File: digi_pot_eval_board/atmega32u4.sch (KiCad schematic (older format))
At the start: 39 parts, among them J3 47346-0001, J4 DS-210, J5 DIN-5-OOTDTY, J6 DIN-5-OOTDTY, J7 JST-04, J8 DS1013-06S, Q1 BSS84, Q2 BSS84, U10 6N138, U11 NCP1117ST50T3G, U12 ATmega32U4-AU, U9 USBLC6-2SC6, Y1 16MHz HC-49SM

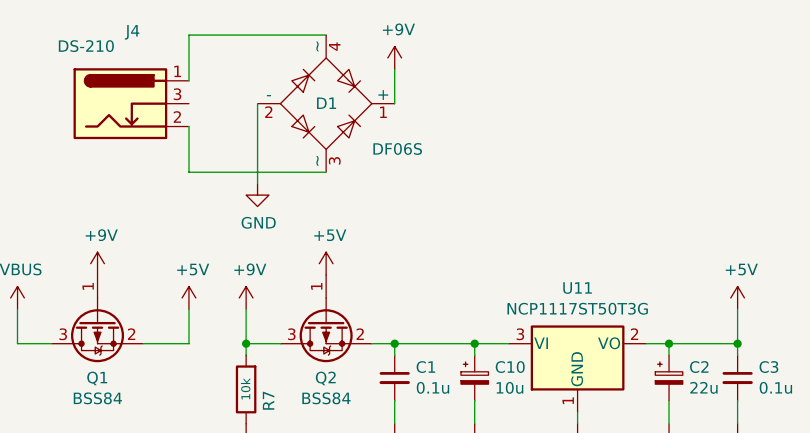
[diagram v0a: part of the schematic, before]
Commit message: Fixing MIDI optocoupler protection diode footprint.
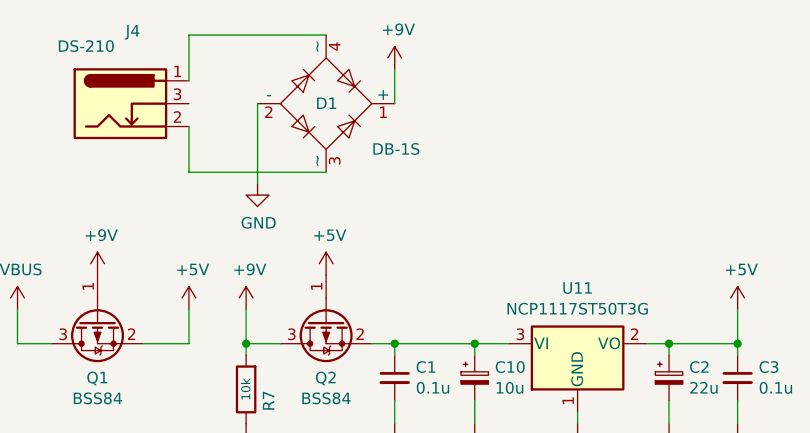
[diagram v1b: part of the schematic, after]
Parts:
- D1: value DF06S -> DB-1S
- D2: footprint Diode_SMD:D_SMA_Handsoldering -> Diode_SMD:D_SMA
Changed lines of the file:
@@
 EESchema Schematic File Version 4
-LIBS:digi_pot_eval_board-cache
 EELAYER 26 0
 EELAYER END
@@
 P 2200 1200
 F 0 "D1" H 2250 1200 50  0000 R CNN
-F 1 "DF06S" H 2400 1400 50  0000 L CNN
+F 1 "DB-1S" H 2400 1400 50  0000 L CNN
 F 2 "Diode_SMD:Diode_Bridge_Vishay_DFS" H 2200 1200 50  0001 C CNN
 F 3 "~" H 2200 1200 50  0001 C CNN
@@
 F 0 "D2" V 2304 5529 50  0000 L CNN
 F 1 "HS1D" V 2395 5529 50  0000 L CNN
-F 2 "Diode_SMD:D_SMA_Handsoldering" H 2350 5450 50  0001 C CNN
+F 2 "Diode_SMD:D_SMA" H 2350 5450 50  0001 C CNN
 F 3 "~" H 2350 5450 50  0001 C CNN
 	1    2350 5450

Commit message: Before wide nav_panel and Level pot move.
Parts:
- added J11: Conn_01x02_Male, Connector_JST:JST_EH_B02B-EH-A_1x02_P2.50mm_Vertical, symbol Connector:Conn_01x02_Male
- added J12: Conn_01x03_Male, Connector_JST:JST_EH_B03B-EH-A_1x03_P2.50mm_Vertical, symbol Connector:Conn_01x03_Male
- added J13: Conn_01x06_Male, Connector_JST:JST_EH_B06B-EH-A_1x06_P2.50mm_Vertical, symbol Connector:Conn_01x06_Male
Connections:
- net labels added: MIN4, MIN5, MOUT4, MOUT5
- wire segments 109 -> 118
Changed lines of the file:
@@
 EESchema Schematic File Version 4
+LIBS:digi_pot_eval_board-cache
 EELAYER 26 0
 EELAYER END
@@
 Wire Wire Line
 	2850 2500 2850 2600
+Text GLabel 1300 5300 0    50   Input ~ 0
+MIN5
+Text GLabel 2000 5300 3    50   Input ~ 0
+MIN4
+Wire Wire Line
+	1300 5300 1400 5300
+Connection ~ 1400 5300
+Text GLabel 4800 5500 3    50   Input ~ 0
+MOUT5
+Text GLabel 5400 5500 3    50   Input ~ 0
+MOUT4
+Wire Wire Line
+	4800 5500 4800 5400
+Connection ~ 4800 5400
+Wire Wire Line
+	5400 5500 5400 5400
+Connection ~ 5400 5400
+$Comp
+L Connector:Conn_01x02_Male J11
+U 1 1 5DB1A299
+P 1600 6100
+F 0 "J11" H 1706 6278 50  0000 C CNN
+F 1 "Conn_01x02_Male" H 1706 6187 50  0000 C CNN
+F 2 "Connector_JST:JST_EH_B02B-EH-A_1x02_P2.50mm_Vertical" H 1600 6100 50  0001 C CNN
+F 3 "~" H 1600 6100 50  0001 C CNN
+	1    1600 6100
+	1    0    0    -1
+$EndComp
+$Comp
+L Connector:Conn_01x03_Male J12
+U 1 1 5DB1A3AD
+P 4900 6300
+F 0 "J12" H 5006 6578 50  0000 C CNN
+F 1 "Conn_01x03_Male" H 5006 6487 50  0000 C CNN
+F 2 "Connector_JST:JST_EH_B03B-EH-A_1x03_P2.50mm_Vertical" H 4900 6300 50  0001 C CNN
+F 3 "~" H 4900 6300 50  0001 C CNN
+	1    4900 6300
+	1    0    0    -1
+$EndComp
+Text GLabel 6300 4050 2    50   Input ~ 0
+MOSI
+Text GLabel 6300 4150 2    50   Input ~ 0
+MISO
+Text GLabel 6300 4250 2    50   Input ~ 0
+SCK
+$Comp
+L Connector:Conn_01x06_Male J13
+U 1 1 5DB1DFAE
+P 6100 4250
+F 0 "J13" H 6206 4628 50  0000 C CNN
+F 1 "Conn_01x06_Male" H 6206 4537 50  0000 C CNN
+F 2 "Connector_JST:JST_EH_B06B-EH-A_1x06_P2.50mm_Vertical" H 6100 4250 50  0001 C CNN
+F 3 "~" H 6100 4250 50  0001 C CNN
+	1    6100 4250
+	1    0    0    -1
+$EndComp
+$Comp
+L power:+5V #PWR0180
+U 1 1 5DB1E025
+P 6800 4350
+F 0 "#PWR0180" H 6800 4200 50  0001 C CNN
+F 1 "+5V" H 6815 4523 50  0000 C CNN
+F 2 "" H 6800 4350 50  0001 C CNN
+F 3 "" H 6800 4350 50  0001 C CNN
+	1    6800 4350
+	1    0    0    -1
+$EndComp
+$Comp
+L power:GND #PWR0181
+U 1 1 5DB1E084
+P 6800 4600
+F 0 "#PWR0181" H 6800 4350 50  0001 C CNN
+F 1 "GND" H 6805 4427 50  0000 C CNN
+F 2 "" H 6800 4600 50  0001 C CNN
+F 3 "" H 6800 4600 50  0001 C CNN
+	1    6800 4600
+	1    0    0    -1
+$EndComp
+Wire Wire Line
+	6300 4550 6800 4550
+Wire Wire Line
+	6800 4550 6800 4600
+Wire Wire Line
+	6800 4350 6800 4450
+Wire Wire Line
+	6800 4450 6300 4450
+$Comp
+L power:GND #PWR0182
+U 1 1 5DB24EBB
+P 5550 6450
+F 0 "#PWR0182" H 5550 6200 50  0001 C CNN
+F 1 "GND" H 5555 6277 50  0000 C CNN
+F 2 "" H 5550 6450 50  0001 C CNN
+F 3 "" H 5550 6450 50  0001 C CNN
+	1    5550 6450
+	1    0    0    -1
+$EndComp
+Text GLabel 5100 6200 2    50   Input ~ 0
+MOUT5
+Text GLabel 5100 6400 2    50   Input ~ 0
+MOUT4
+Wire Wire Line
+	5100 6300 5550 6300
+Wire Wire Line
+	5550 6300 5550 6450
+Text GLabel 1800 6100 2    50   Input ~ 0
+MIN5
+Text GLabel 1800 6200 2    50   Input ~ 0
+MIN4
 $EndSCHEMATC

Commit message: Introducing new layout.
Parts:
- removed J11: Conn_01x02_Male, Connector_JST:JST_EH_B02B-EH-A_1x02_P2.50mm_Vertical, symbol Connector:Conn_01x02_Male
- removed J12: Conn_01x03_Male, Connector_JST:JST_EH_B03B-EH-A_1x03_P2.50mm_Vertical, symbol Connector:Conn_01x03_Male
- added J10: Conn_01x02_Male, Connector_JST:JST_EH_B02B-EH-A_1x02_P2.50mm_Vertical, symbol Connector:Conn_01x02_Male
- added J9: Conn_01x05_Male, Connector_JST:JST_EH_B05B-EH-A_1x05_P2.50mm_Vertical, symbol Connector:Conn_01x05_Male
- J4: footprint Connector_BarrelJack:BarrelJack_Wuerth_6941xx301002 -> (none)
- J5, J6: footprint Connectors:DIN5MIDI-OOTDTY -> (none)
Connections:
- net labels added: POW1, POW2
- wire segments 118 -> 120
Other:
- moved on the sheet: J4
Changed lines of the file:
@@
 L Connector:Barrel_Jack_Switch J4
 U 1 1 5D90FDCF
-P 1300 1200
-F 0 "J4" H 1355 1517 50  0000 C CNN
-F 1 "DS-210" H 1150 1450 50  0000 C CNN
-F 2 "Connector_BarrelJack:BarrelJack_Wuerth_6941xx301002" H 1350 1160 50  0001 C CNN
-F 3 "~" H 1350 1160 50  0001 C CNN
-	1    1300 1200
+P 900 1200
+F 0 "J4" H 955 1517 50  0000 C CNN
+F 1 "DS-210" H 750 1450 50  0000 C CNN
+F 2 "" H 950 1160 50  0001 C CNN
+F 3 "~" H 950 1160 50  0001 C CNN
+	1    900  1200
 	1    0    0    -1
 $EndComp
@@
 F 0 "J6" H 5100 4933 50  0000 C CNN
 F 1 "DIN-5-OOTDTY" H 5100 5024 50  0000 C CNN
-F 2 "Connectors:DIN5MIDI-OOTDTY" H 5100 5300 50  0001 C CNN
+F 2 "" H 5100 5300 50  0001 C CNN
 F 3 "http://www.mouser.com/ds/2/18/40_c091_abd_e-75918.pdf" H 5100 5300 50  0001 C CNN
 	1    5100 5300
@@
 F 0 "J5" H 1700 4833 50  0000 C CNN
 F 1 "DIN-5-OOTDTY" H 1700 4924 50  0000 C CNN
-F 2 "Connectors:DIN5MIDI-OOTDTY" H 1700 5200 50  0001 C CNN
+F 2 "" H 1700 5200 50  0001 C CNN
 F 3 "http://www.mouser.com/ds/2/18/40_c091_abd_e-75918.pdf" H 1700 5200 50  0001 C CNN
 	1    1700 5200
@@
 	5400 5500 5400 5400
 Connection ~ 5400 5400
-$Comp
-L Connector:Conn_01x02_Male J11
-U 1 1 5DB1A299
-P 1600 6100
-F 0 "J11" H 1706 6278 50  0000 C CNN
-F 1 "Conn_01x02_Male" H 1706 6187 50  0000 C CNN
-F 2 "Connector_JST:JST_EH_B02B-EH-A_1x02_P2.50mm_Vertical" H 1600 6100 50  0001 C CNN
-F 3 "~" H 1600 6100 50  0001 C CNN
-	1    1600 6100
-	1    0    0    -1
-$EndComp
-$Comp
-L Connector:Conn_01x03_Male J12
-U 1 1 5DB1A3AD
-P 4900 6300
-F 0 "J12" H 5006 6578 50  0000 C CNN
-F 1 "Conn_01x03_Male" H 5006 6487 50  0000 C CNN
-F 2 "Connector_JST:JST_EH_B03B-EH-A_1x03_P2.50mm_Vertical" H 4900 6300 50  0001 C CNN
-F 3 "~" H 4900 6300 50  0001 C CNN
-	1    4900 6300
-	1    0    0    -1
-$EndComp
 Text GLabel 6300 4050 2    50   Input ~ 0
 MOSI
@@
 Wire Wire Line
 	6800 4450 6300 4450
+Text GLabel 1550 1100 0    50   Input ~ 0
+POW1
+Wire Wire Line
+	1550 1100 1600 1100
+Text GLabel 1550 1300 0    50   Input ~ 0
+POW2
+Wire Wire Line
+	1550 1300 1600 1300
+$Comp
+L Connector:Conn_01x02_Male J10
+U 1 1 5DB811AD
+P 3650 1100
+F 0 "J10" H 3756 1278 50  0000 C CNN
+F 1 "Conn_01x02_Male" H 3756 1187 50  0000 C CNN
+F 2 "Connector_JST:JST_EH_B02B-EH-A_1x02_P2.50mm_Vertical" H 3650 1100 50  0001 C CNN
+F 3 "~" H 3650 1100 50  0001 C CNN
+	1    3650 1100
+	-1   0    0    -1
+$EndComp
+Text GLabel 3450 1100 0    50   Input ~ 0
+POW1
+Text GLabel 3450 1200 0    50   Input ~ 0
+POW2
+$Comp
+L Connector:Conn_01x05_Male J9
+U 1 1 5DB82855
+P 2700 6750
+F 0 "J9" H 2806 7128 50  0000 C CNN
+F 1 "Conn_01x05_Male" H 2806 7037 50  0000 C CNN
+F 2 "Connector_JST:JST_EH_B05B-EH-A_1x05_P2.50mm_Vertical" H 2700 6750 50  0001 C CNN
+F 3 "~" H 2700 6750 50  0001 C CNN
+	1    2700 6750
+	1    0    0    -1
+$EndComp
+Text GLabel 2900 6850 2    50   Input ~ 0
+MIN5
+Text GLabel 2900 6950 2    50   Input ~ 0
+MIN4
+Text GLabel 2900 6550 2    50   Input ~ 0
+MOUT5
+Text GLabel 2900 6750 2    50   Input ~ 0
+MOUT4
 $Comp
 L power:GND #PWR0182
-U 1 1 5DB24EBB
-P 5550 6450
-F 0 "#PWR0182" H 5550 6200 50  0001 C CNN
-F 1 "GND" H 5555 6277 50  0000 C CNN
-F 2 "" H 5550 6450 50  0001 C CNN
-F 3 "" H 5550 6450 50  0001 C CNN
-	1    5550 6450
-	1    0    0    -1
-$EndComp
-Text GLabel 5100 6200 2    50   Input ~ 0
-MOUT5
-Text GLabel 5100 6400 2    50   Input ~ 0
-MOUT4
-Wire Wire Line
-	5100 6300 5550 6300
-Wire Wire Line
-	5550 6300 5550 6450
-Text GLabel 1800 6100 2    50   Input ~ 0
-MIN5
-Text GLabel 1800 6200 2    50   Input ~ 0
-MIN4
+U 1 1 5DB82A46
+P 3400 6700
+F 0 "#PWR0182" H 3400 6450 50  0001 C CNN
+F 1 "GND" H 3405 6527 50  0000 C CNN
+F 2 "" H 3400 6700 50  0001 C CNN
+F 3 "" H 3400 6700 50  0001 C CNN
+	1    3400 6700
+	1    0    0    -1
+$EndComp
+Wire Wire Line
+	2900 6650 3400 6650
+Wire Wire Line
+	3400 6650 3400 6700
 $EndSCHEMATC

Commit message: Printed and tested layout version.
USB still on upper board.
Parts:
- removed D3: LED, LED_THT:LED_D5.0mm, symbol Device:LED
- removed J3: 47346-0001, Connector_USB:USB_Micro-B_Molex_47346-0001, symbol Connector:USB_B_Micro
- removed J4: DS-210, symbol Connector:Barrel_Jack_Switch
- removed J7: JST-04, Connector_JST:JST_EH_B04B-EH-A_1x04_P2.50mm_Vertical, symbol Connector:Conn_01x04_Male
- added J11, J12, J7: Conn_01x02_Male, Connector_JST:JST_EH_B02B-EH-A_1x02_P2.50mm_Vertical, symbol Connector:Conn_01x02_Male
- added J3: USB_B, Connector_USB:USB_B_OST_USB-B1HSxx_Horizontal, symbol Connector:USB_B
- added JP1, JP2, JP3: Jumper_NC_Small, Connector_PinHeader_2.54mm:PinHeader_1x02_P2.54mm_Vertical, symbol Device:Jumper_NC_Small
- added R2: 10k, Resistor_SMD:R_0805_2012Metric_Pad1.15x1.40mm_HandSolder, symbol Device:R
- added SW1: SW_MEC_5G_LED, bypass_panel:bypass_panel_THT, symbol Switch:SW_MEC_5G_LED
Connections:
- net labels added: BYPASS_LED, BYP_L+, BYP_L-, BYP_SW1, SW_BYPASS
- net labels removed: PASSBACK_LED, SW_PASSBACK
- wire segments 120 -> 128
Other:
- moved on the sheet: R1

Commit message: Production version 2019.11.19.
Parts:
- added J14: Conn_01x02_Male, Connector_JST:JST_EH_B02B-EH-A_1x02_P2.50mm_Vertical, symbol Connector:Conn_01x02_Male
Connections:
- net labels added: D_CS
- wire segments 128 -> 131
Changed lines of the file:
@@
 	5400 5500 5400 5400
 Connection ~ 5400 5400
-Text GLabel 6300 4050 2    50   Input ~ 0
+Text GLabel 6300 4450 2    50   Input ~ 0
 MOSI
-Text GLabel 6300 4150 2    50   Input ~ 0
+Text GLabel 6300 4350 2    50   Input ~ 0
 MISO
 Text GLabel 6300 4250 2    50   Input ~ 0
@@
 L power:+5V #PWR0180
 U 1 1 5DB1E025
-P 6800 4350
-F 0 "#PWR0180" H 6800 4200 50  0001 C CNN
-F 1 "+5V" H 6815 4523 50  0000 C CNN
-F 2 "" H 6800 4350 50  0001 C CNN
-F 3 "" H 6800 4350 50  0001 C CNN
-	1    6800 4350
+P 6800 4150
+F 0 "#PWR0180" H 6800 4000 50  0001 C CNN
+F 1 "+5V" H 6815 4323 50  0000 C CNN
+F 2 "" H 6800 4150 50  0001 C CNN
+F 3 "" H 6800 4150 50  0001 C CNN
+	1    6800 4150
 	1    0    0    -1
 $EndComp
@@
 L power:GND #PWR0181
 U 1 1 5DB1E084
-P 6800 4600
-F 0 "#PWR0181" H 6800 4350 50  0001 C CNN
-F 1 "GND" H 6805 4427 50  0000 C CNN
-F 2 "" H 6800 4600 50  0001 C CNN
-F 3 "" H 6800 4600 50  0001 C CNN
-	1    6800 4600
-	1    0    0    -1
-$EndComp
-Wire Wire Line
-	6300 4550 6800 4550
-Wire Wire Line
-	6800 4550 6800 4600
-Wire Wire Line
-	6800 4350 6800 4450
-Wire Wire Line
-	6800 4450 6300 4450
+P 6650 4000
+F 0 "#PWR0181" H 6650 3750 50  0001 C CNN
+F 1 "GND" H 6655 3827 50  0000 C CNN
+F 2 "" H 6650 4000 50  0001 C CNN
+F 3 "" H 6650 4000 50  0001 C CNN
+	1    6650 4000
+	-1   0    0    1
+$EndComp
+Text GLabel 1550 1300 0    50   Input ~ 0
+POW1
+Wire Wire Line
+	1550 1100 1600 1100
 Text GLabel 1550 1100 0    50   Input ~ 0
-POW1
-Wire Wire Line
-	1550 1100 1600 1100
-Text GLabel 1550 1300 0    50   Input ~ 0
 POW2
 Wire Wire Line
@@
 F 3 "~" H 6300 6050 50  0001 C CNN
 	1    6300 6050
-	0    -1   -1   0
-$EndComp
-Wire Wire Line
-	6500 5950 6300 5950
+	0    -1   1    0
+$EndComp
 $Comp
 L Device:Jumper_NC_Small JP3
@@
 Wire Wire Line
 	7050 5650 7300 5650
-Connection ~ 6300 5950
 Text GLabel 6200 5950 0    50   Input ~ 0
 BYP_L-
-Wire Wire Line
-	6200 5950 6300 5950
 Wire Wire Line
 	6250 6150 6300 6150
@@
 L Connector:Conn_01x02_Male J7
 U 1 1 5DCA85C1
-P 4600 1100
-F 0 "J7" H 4706 1278 50  0000 C CNN
-F 1 "Conn_01x02_Male" H 4706 1187 50  0000 C CNN
-F 2 "Connector_JST:JST_EH_B02B-EH-A_1x02_P2.50mm_Vertical" H 4600 1100 50  0001 C CNN
-F 3 "~" H 4600 1100 50  0001 C CNN
-	1    4600 1100
-	-1   0    0    -1
+P 4600 1200
+F 0 "J7" H 4706 1378 50  0000 C CNN
+F 1 "Conn_01x02_Male" H 4706 1287 50  0000 C CNN
+F 2 "Connector_JST:JST_EH_B02B-EH-A_1x02_P2.50mm_Vertical" H 4600 1200 50  0001 C CNN
+F 3 "~" H 4600 1200 50  0001 C CNN
+	1    4600 1200
+	-1   0    0    1
 $EndComp
 $Comp
@@
 $EndComp
 $Comp
-L power:GND #PWR?
+L power:GND #PWR0183
 U 1 1 5DCDA9CD
 P 5500 6850
-F 0 "#PWR?" H 5500 6600 50  0001 C CNN
+F 0 "#PWR0183" H 5500 6600 50  0001 C CNN
 F 1 "GND" H 5505 6677 50  0000 C CNN
 F 2 "" H 5500 6850 50  0001 C CNN
@@
 Wire Wire Line
 	3350 6850 3350 6950
+Wire Wire Line
+	6200 5950 6300 5950
+Connection ~ 6300 5950
+Wire Wire Line
+	6300 5950 6500 5950
+Wire Wire Line
+	6300 4050 6650 4050
+Wire Wire Line
+	6650 4050 6650 4000
+Wire Wire Line
+	6300 4150 6800 4150
+Text GLabel 6300 4550 2    50   Input ~ 0
+D_CS
+Text GLabel 9500 2700 2    50   Input ~ 0
+D_CS
+$Comp
+L Connector:Conn_01x02_Male J14
+U 1 1 5DD42436
+P 5700 1200
+F 0 "J14" H 5806 1378 50  0000 C CNN
+F 1 "Conn_01x02_Male" H 5806 1287 50  0000 C CNN
+F 2 "Connector_JST:JST_EH_B02B-EH-A_1x02_P2.50mm_Vertical" H 5700 1200 50  0001 C CNN
+F 3 "~" H 5700 1200 50  0001 C CNN
+	1    5700 1200
+	-1   0    0    1
+$EndComp
+$Comp
+L power:GND #PWR0184
+U 1 1 5DD4255E
+P 5200 1250
+F 0 "#PWR0184" H 5200 1000 50  0001 C CNN
+F 1 "GND" H 5205 1077 50  0000 C CNN
+F 2 "" H 5200 1250 50  0001 C CNN
+F 3 "" H 5200 1250 50  0001 C CNN
+	1    5200 1250
+	1    0    0    -1
+$EndComp
+$Comp
+L power:+5V #PWR0185
+U 1 1 5DD425C9
+P 5200 1050
+F 0 "#PWR0185" H 5200 900 50  0001 C CNN
+F 1 "+5V" H 5215 1223 50  0000 C CNN
+F 2 "" H 5200 1050 50  0001 C CNN
+F 3 "" H 5200 1050 50  0001 C CNN
+	1    5200 1050
+	1    0    0    -1
+$EndComp
+Wire Wire Line
+	5200 1050 5200 1100
+Wire Wire Line
+	5200 1100 5500 1100
+Wire Wire Line
+	5500 1200 5200 1200
+Wire Wire Line
+	5200 1200 5200 1250
 $EndSCHEMATC

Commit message: Upgrading KiCad and fixing ULN2003a connection.
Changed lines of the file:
@@
 EESchema Schematic File Version 4
-LIBS:digi_pot_eval_board-cache
-EELAYER 26 0
+EELAYER 30 0
 EELAYER END
 $Descr A4 11693 8268
@@
 $Comp
 L MCU_Microchip_ATmega:ATmega32U4-AU U12
-U 1 1 5D8E6AD7
+U 1 1 5E17DEF9
 P 8900 3500
-F 0 "U12" H 8500 5300 50  0000 C CNN
-F 1 "ATmega32U4-AU" H 9450 1700 50  0000 C CNN
+F 0 "U12" H 9300 5300 50  0000 C CNN
+F 1 "ATmega32U4-AU" H 8850 3450 50  0000 C CNN
 F 2 "Package_QFP:TQFP-44_10x10mm_P0.8mm" H 8900 3500 50  0001 C CIN
 F 3 "http://ww1.microchip.com/downloads/en/DeviceDoc/Atmel-7766-8-bit-AVR-ATmega16U4-32U4_Datasheet.pdf" H 8900 3500 50  0001 C CNN
